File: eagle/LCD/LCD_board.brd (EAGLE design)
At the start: 93.1 x 60.1 mm, 7 parts, among them CN1 1X4-CLEANBIG

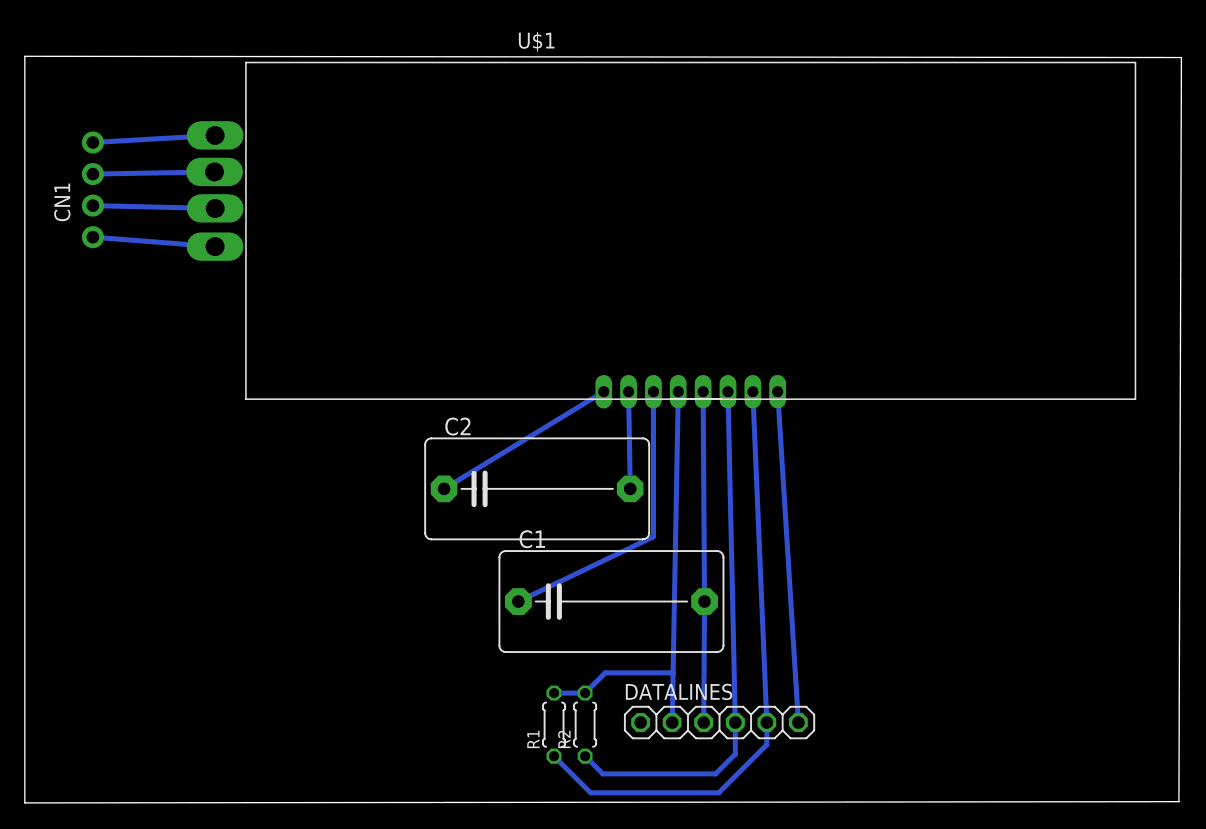
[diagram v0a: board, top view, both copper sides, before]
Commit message: Updated LCD board with surface mount components and a 2x4 header connector
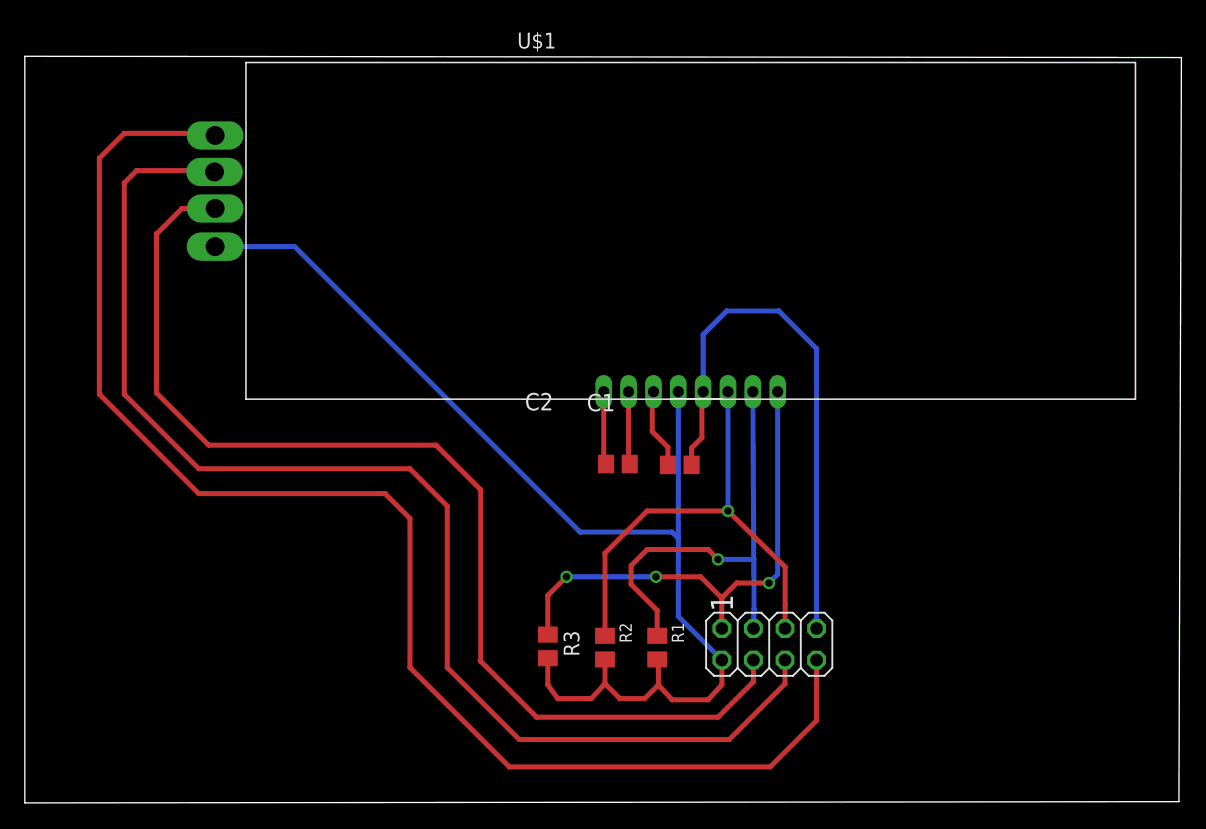
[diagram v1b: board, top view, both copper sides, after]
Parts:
- removed CN1: 1X4-CLEANBIG, adafruit:1X04-CLEANBIG
- added R3: 10k, T06_LockBox:M0805
- C1, C2: device capacitor-wima:C15B8 -> T06_LockBox:C0805
- DATALINES: device adafruit:1X06 -> T06_LockBox:2X04
- R1, R2: device T06_LockBox:0204/5 -> T06_LockBox:M0805
- moved C1 12.3 mm to (52.7, 27.3)
- moved R1 10.4 mm to (50.9, 12.6), turned to 270 degrees
- moved DATALINES 7.46 mm to (59.9, 12.9)
- moved C2 6.80 mm to (47.7, 27.4)
- moved R2 6.40 mm to (46.7, 12.6), turned to 270 degrees
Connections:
- removed net A: CN1.4, U$1.P$RK
- removed net GK: CN1.2, U$1.P$BK
- removed net N$2: CN1.3, U$1.P$GK
- removed net N$4: CN1.1, U$1.P$A
- removed net RST: DATALINES.6, U$1.P$1
- new net K-B: DATALINES.3, U$1.P$BK
- new net K-G: DATALINES.5, U$1.P$GK
- new net K-R: DATALINES.7, U$1.P$RK
- new net N$6: DATALINES.2, R3.1, U$1.P$1
- net GND: now also DATALINES.8; no longer DATALINES.1, DATALINES.3
- net SCL: now also DATALINES.4; no longer DATALINES.5
- net SDA: now also DATALINES.6; no longer DATALINES.4
- net VDD: now also DATALINES.1, R3.2, U$1.P$A; no longer DATALINES.2
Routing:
- net K-R: track 0.00 -> 112.8 mm
- net K-G: track 0.00 -> 100.8 mm
- net K-B: track 0.00 -> 88.2 mm
- net VDD: track 36.9 -> 95.4 mm
- net N$6: track 0.00 -> 40.9 mm, vias 0 -> 3
- net RST: track 26.7 -> 0.00 mm
- net GND: track 26.6 -> 44.6 mm
- net N$5: track 23.7 -> 6.46 mm
- net SCL: track 48.4 -> 36.3 mm, vias 0 -> 1
- net N$4: track 9.86 -> 0.00 mm
- net A: track 9.85 -> 0.00 mm
- net GK: track 9.84 -> 0.00 mm
- net N$2: track 9.79 -> 0.00 mm
- net N$1: track 15.0 -> 6.01 mm
- net SDA: track 42.5 -> 39.0 mm, vias 0 -> 1
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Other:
- board text added: "1"

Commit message: Created 2 layer LDC board with smaller footprint than previous versions
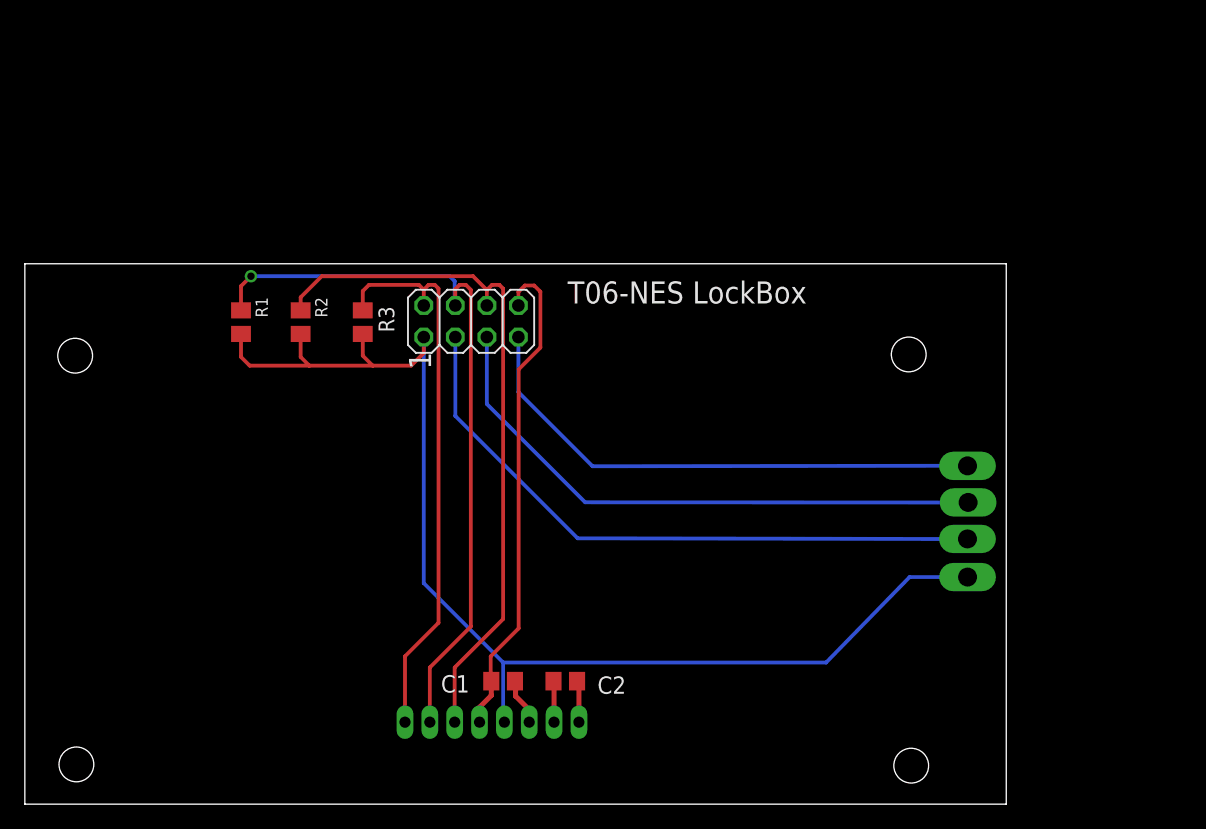
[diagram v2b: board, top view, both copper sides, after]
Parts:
- moved R1 42.5 mm to (17.4, 38.8)
- moved R2 35.9 mm to (22.2, 38.8)
- moved DATALINES 35.4 mm to (35.9, 38.9)
- moved U$1 31.0 mm to (37.6, 22.8), flipped to the bottom
- moved R3 30.1 mm to (27.2, 38.8)
- moved C1 22.5 mm to (38.5, 9.90), turned to 180 degrees
- moved C2 18.0 mm to (43.5, 9.90), turned to 180 degrees
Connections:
- net K-B renamed EN_BL
- net K-G renamed EN_G
- net K-R renamed EN_RD
- net N$6 renamed !LCD_RST
- net VDD renamed 3.3V
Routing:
- net EN_RD: track 112.8 -> 43.1 mm
- net EN_G: track 100.8 -> 47.4 mm
- net EN_BL: track 88.2 -> 51.7 mm
- net SCL: track 36.3 -> 60.7 mm
- net SDA: track 39.0 -> 56.6 mm, vias 1 -> 0
- net !LCD_RST: track 40.9 -> 45.6 mm, vias 3 -> 0
- net GND: track 44.6 -> 40.0 mm
- net 3.3V: track 95.4 -> 98.3 mm
- net N$5: track 6.46 -> 3.78 mm
- net N$1: track 6.01 -> 3.45 mm
- net C1+: track 5.91 -> 3.35 mm
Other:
- board size 93.1 x 60.1 mm -> 79 x 43.5 mm
- board text added: "T06-NES LockBox"
